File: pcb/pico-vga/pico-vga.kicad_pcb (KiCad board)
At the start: 2 copper layers, 84 x 103 mm, 68 parts, among them J1 DB15_Female_HighDensity, J2 Micro_SD_Card, J3 AudioJack3, J4 USB_C_Receptacle, J5 USB_C_Receptacle, J6 USB_C_Receptacle, J7 USB_C_Receptacle, J8 USB_C_Receptacle, SW1 SW_Push, U1 Raspberry_Pi_Pico, U10 SN74LVC08A, U11 SN74LVC08A, U12 SN74LVC08A, U13 CD4072B, U14 CD4072B, U15 CD4072B, U16 CD4072B, U2 74LVC2G34, U3 74LVC04A, U4 SN74LVC139A, U5 SN74LVC08A, U6 SN74LVC08A, U7 SN74LVC08A, U8 SN74LVC08A, U9 SN74LVC08A

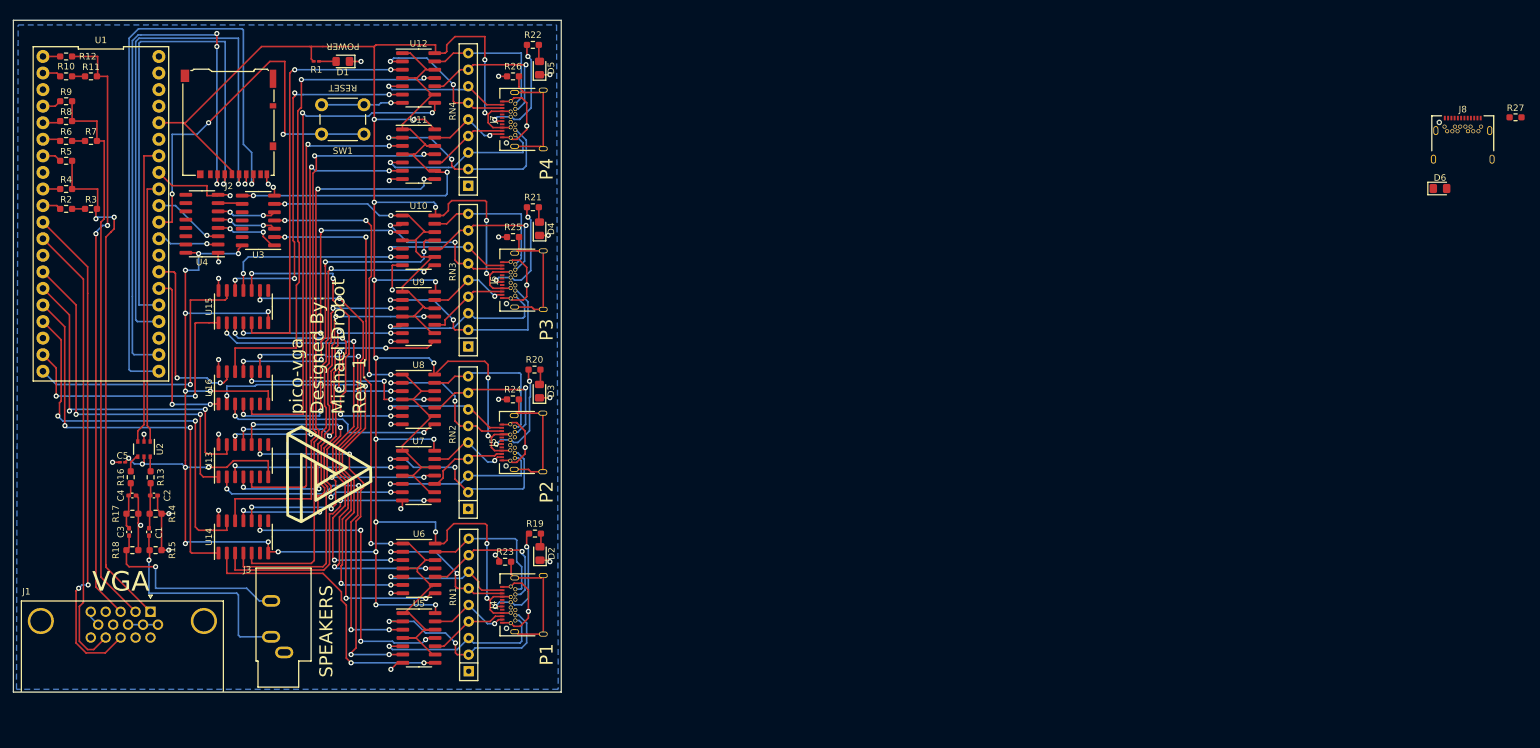
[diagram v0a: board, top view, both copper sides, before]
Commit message: Pico-VGA and Controller PCBs DONE!
Updates to pico-vga: I don't remember.... Uhhh.... I did stuff? Whatever, I like the layout, it passes DRC, it's badged, and it now has mounting holes. Updates to controller: It now exists. It also passes DRC, now has rounded corners, and has mounting holes. I'm using custom combination THT/SMD footprints for the buttons, so you can use either one depending on what you buy
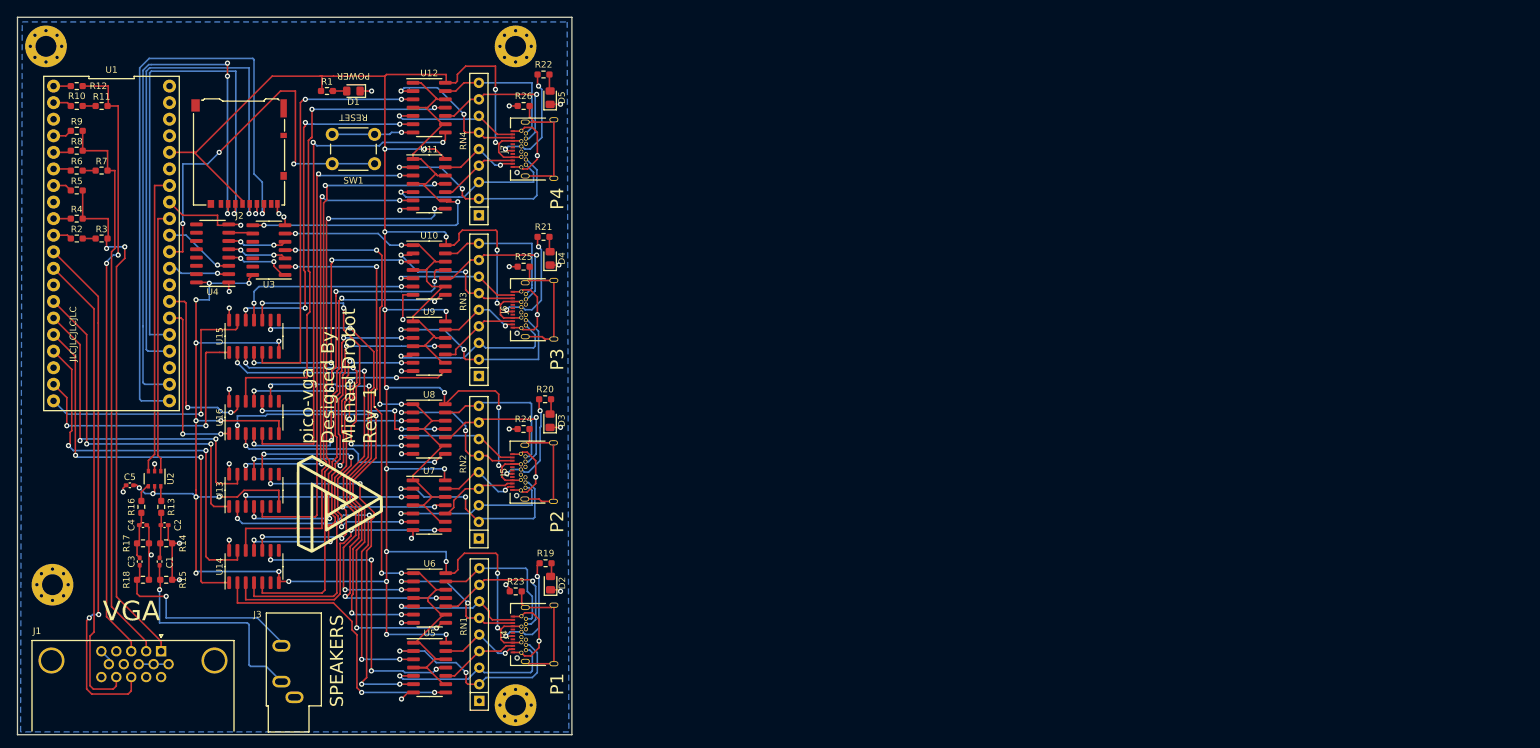
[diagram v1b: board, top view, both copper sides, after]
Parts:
- removed D6: LED, LED_SMD:LED_0805_2012Metric_Pad1.15x1.40mm_HandSolder
- removed J8: USB_C_Receptacle, pico-vga:USB_C_Receptacle_Molex_2171830001
- removed R27: 1K, Resistor_SMD:R_0603_1608Metric_Pad0.98x0.95mm_HandSolder
- added REF**: MountingHole_3.2mm_M3_Pad_Via, MountingHole:MountingHole_3.2mm_M3_Pad_Via, F.Cu at (91.0, 118.0)
- added REF**: MountingHole_3.2mm_M3_Pad_Via, MountingHole:MountingHole_3.2mm_M3_Pad_Via, F.Cu at (19.0, 17.0)
- added REF**: MountingHole_3.2mm_M3_Pad_Via, MountingHole:MountingHole_3.2mm_M3_Pad_Via, F.Cu at (91.0, 17.0)
- added REF**: MountingHole_3.2mm_M3_Pad_Via, MountingHole:MountingHole_3.2mm_M3_Pad_Via, F.Cu at (20.0, 99.5)
- C5: footprint Capacitor_SMD:C_0201_0603Metric_Pad0.64x0.40mm_HandSolder -> Capacitor_SMD:C_0402_1005Metric_Pad0.74x0.62mm_HandSolder
- R1: footprint Resistor_SMD:R_0201_0603Metric_Pad0.64x0.40mm_HandSolder -> Resistor_SMD:R_0603_1608Metric_Pad0.98x0.95mm_HandSolder
- moved J3 7.06 mm to (57.1, 116.8)
- moved J1 6.27 mm to (36.7, 109.7)
- moved C2 4.82 mm to (37.2, 90.4)
- moved C4 4.82 mm to (33.9, 90.4)
- moved D1 4.82 mm to (66.1, 23.9)
- moved D2 4.82 mm to (96.4, 99.3)
- moved D3 4.82 mm to (96.3, 74.4)
- moved D4 4.82 mm to (96.3, 49.5)
- moved J2 4.82 mm to (48.6, 33.4)
- moved J4 4.82 mm to (95.6, 107.2)
- moved J5 4.82 mm to (95.5, 82.3)
- moved J6 4.82 mm to (95.6, 57.4)
- moved R1 4.82 mm to (62.1, 23.8)
- moved R13 4.82 mm to (36.7, 87.6)
- moved R14 4.82 mm to (37.4, 93.2)
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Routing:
- net /HSYNC: track 77.1 -> 80.7 mm
- net /VSYNC: track 69.9 -> 72.6 mm
- net Net-(J1-Pad3): track 93.5 -> 95.2 mm
- net Net-(J1-Pad2): track 85.6 -> 87.1 mm
- net Net-(J1-Pad1): track 79.7 -> 81.2 mm
- net Net-(C3-Pad2): track 31.0 -> 32.2 mm
- net Net-(C1-Pad2): track 34.0 -> 35.0 mm
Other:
- board size 84 x 103 mm -> 85 x 110 mm
- board text added: "JLCJLCJLCJLC"

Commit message: moved sd card slot, reset switch, power led
when I added the mounting holes it lengthened the board, and the sd slot, power led, and reset switch were in a pretty bad place. Moved them back to the edge of the board, redid traces, and it passes DRC
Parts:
- moved SW1 19.5 mm to (81.0, 19.3)
- moved J2 11.9 mm to (48.8, 21.5)
- moved D1 9.34 mm to (60.7, 16.3), turned to 0 degrees
- moved R1 8.34 mm to (65.5, 16.3), turned to 180 degrees
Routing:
- net /SD_CS: track 90.1 -> 71.3 mm, vias 3 -> 1
- net /SD_MOSI: track 80.0 -> 63.0 mm
- net /SD_CLK: track 86.2 -> 69.7 mm
- net /SD_MISO: track 99.4 -> 83.3 mm
- net Net-(SW1-Pad1): track 61.1 -> 71.8 mm, vias 3 -> 1
- net GND: track 149.2 -> 142.5 mm, vias 35 -> 34
- net +3V3: track 488.2 -> 491.1 mm

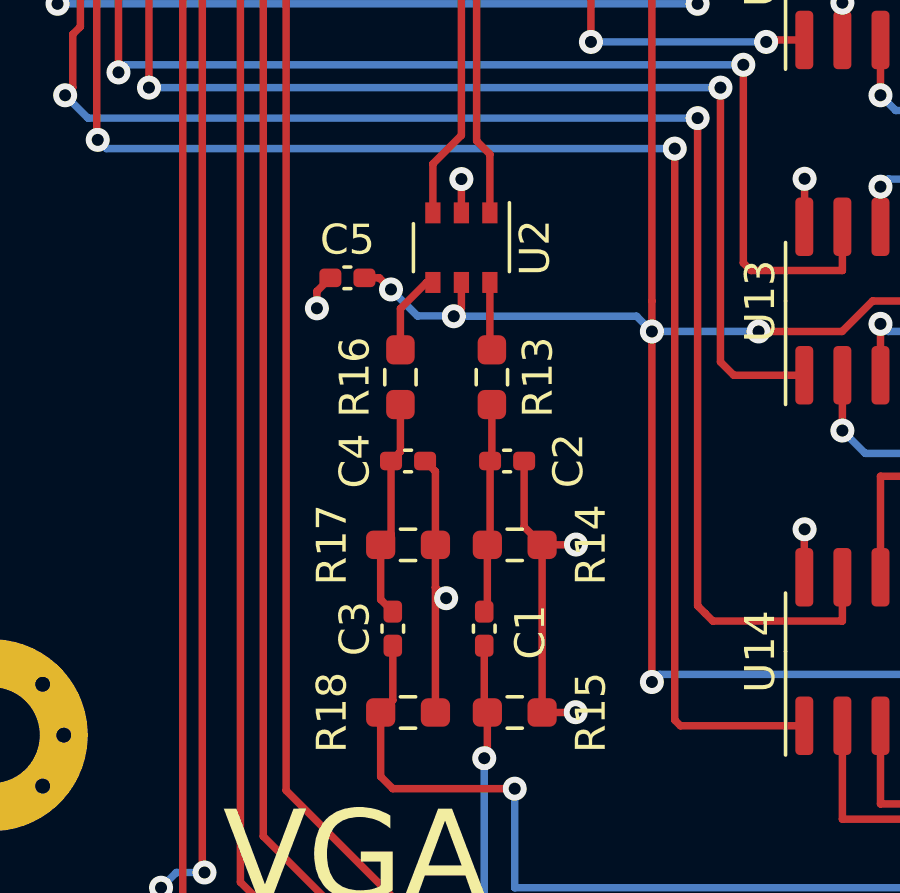
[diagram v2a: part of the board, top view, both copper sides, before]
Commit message: footprint fixes
some parts were not available in the footprint I picked for them, so I had to make some swaps. Also updated BOM doc
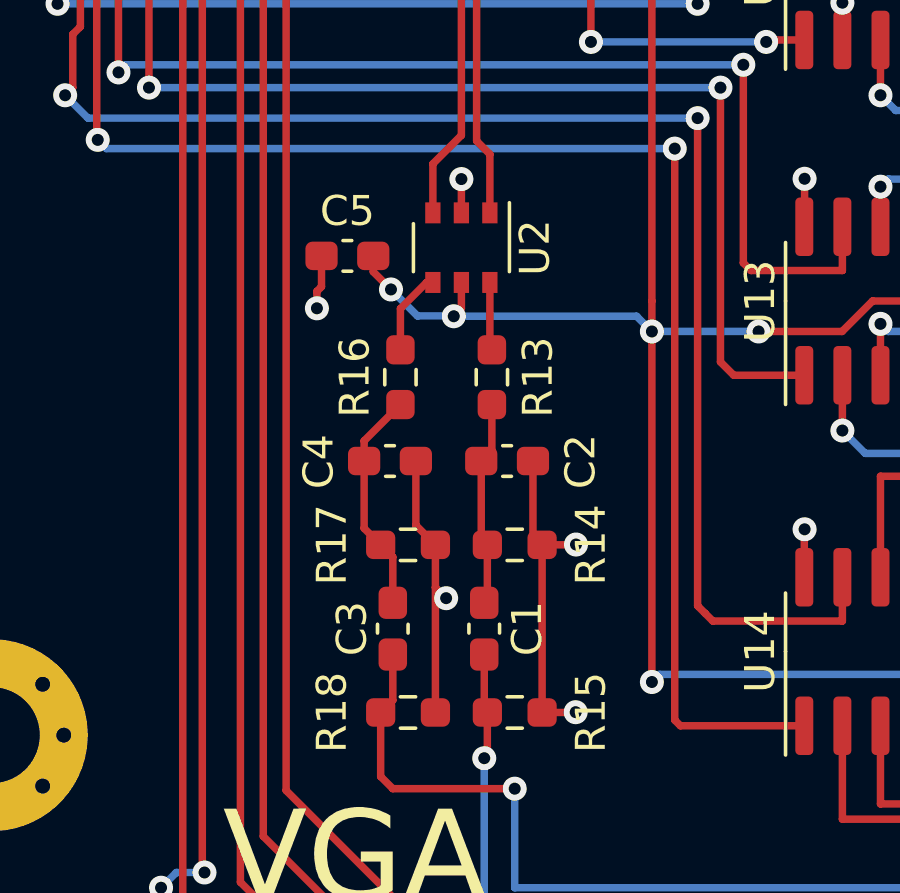
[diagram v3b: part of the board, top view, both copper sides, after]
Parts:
- C1, C2, C3, C4, C5: footprint Capacitor_SMD:C_0402_1005Metric_Pad0.74x0.62mm_HandSolder -> Capacitor_SMD:C_0603_1608Metric_Pad1.08x0.95mm_HandSolder
- moved C5 0.73 mm to (31.9, 83.6)
- moved C4 0.60 mm to (33.3, 90.4)
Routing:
- net GND: track 142.5 -> 143.1 mm

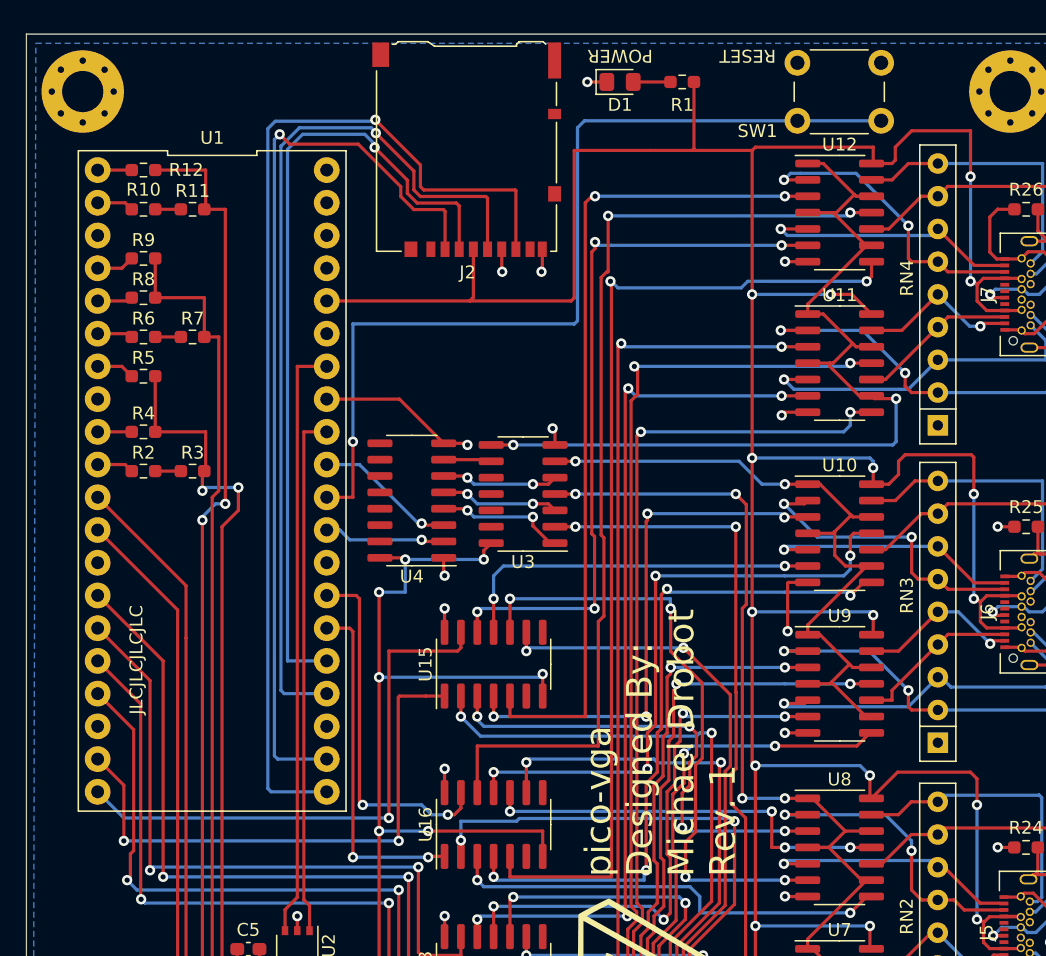
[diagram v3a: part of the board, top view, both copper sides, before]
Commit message: added auxiliary SPI and power headers to pcb
added a header for SPI to the board, so the board can act as a peripheral for other devices, and data/commands can be sent over SPI. also added auxiliary power connector, meant to be used when the board is in peripheral mode.
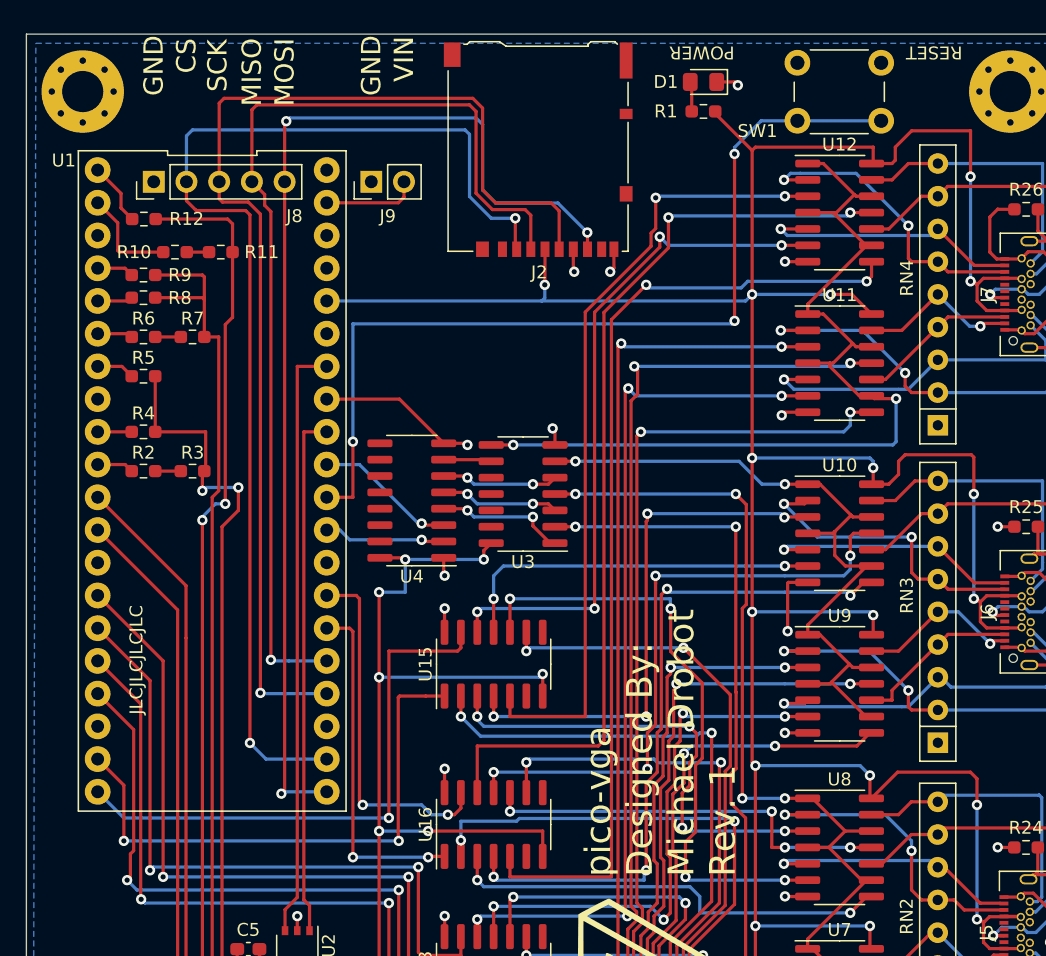
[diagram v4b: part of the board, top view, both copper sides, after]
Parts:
- added J8: Conn_01x05_Male, Connector_PinHeader_2.54mm:PinHeader_1x05_P2.54mm_Vertical, F.Cu at (24.5, 24.0)
- added J9: Conn_01x02_Male, Connector_PinHeader_2.54mm:PinHeader_1x02_P2.54mm_Vertical, F.Cu at (41.4, 24.0)
- moved D1 6.48 mm to (67.2, 16.3), turned to 180 degrees
- moved J2 5.56 mm to (54.4, 21.5)
- moved R10 4.13 mm to (26.2, 29.5)
- moved R11 3.98 mm to (29.7, 29.5)
- moved R12 3.80 mm to (23.7, 26.9)
- moved R1 2.82 mm to (67.2, 18.5)
- moved R9 1.29 mm to (23.7, 31.2)
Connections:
- U1 pad 39: unconnected-(U1-Pad39) -> +5V
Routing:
- net /SD_CLK: track 69.7 -> 90.3 mm
- net /SD_CS: track 71.3 -> 91.7 mm, vias 1 -> 2
- net /SD_MOSI: track 63.0 -> 79.4 mm
- net +3V3: track 491.4 -> 478.9 mm, vias 37 -> 38
- net +5V: track 0.00 -> 7.38 mm
- net /BLUE_1: track 2.85 -> 7.93 mm
- net /SD_MISO: track 83.3 -> 87.4 mm, vias 1 -> 3
- net Net-(J1-Pad3): track 95.2 -> 91.8 mm
- net /ControllerInterface/C4_BTN_Y: track 75.3 -> 72.2 mm
- net /ControllerInterface/C4_BTN_A: track 64.8 -> 61.8 mm
- net Net-(J1-Pad2): track 87.1 -> 89.7 mm
- net /ControllerInterface/C4_BTN_B: track 56.1 -> 53.5 mm
- net /BLUE_2: track 2.64 -> 4.91 mm
- net /ControllerInterface/C4_BTN_X: track 77.7 -> 75.6 mm
- net Net-(SW1-Pad1): track 71.8 -> 70.9 mm, vias 1 -> 3
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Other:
- board text added: "CS"
- board text added: "GND"
- board text added: "MISO"
- board text added: "MOSI"
- board text added: "SCK"
- board text added: "VIN"
- board text added: "VIN: 1.8-5.5VDC"
